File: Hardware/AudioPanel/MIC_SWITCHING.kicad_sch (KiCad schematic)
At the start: 18 parts, among them SW8 ~{RESET}, U119 ADG729, U120 ADG729, U30 MCP23017_ML, U60 MCP23017_ML

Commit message: Added MIC PTT UP DOWN sensing and buffering
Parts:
- removed C141, C142: 100nF, symbol Device:C_Small
- removed C143: 10uF, symbol Device:C_Polarized_Small_US
- removed SW8: ~{RESET}, Button_Switch_SMD:SW_SPST_TL3342, symbol Switch:SW_Push
- removed U30: MCP23017_ML, Package_DFN_QFN:QFN-28-1EP_6x6mm_P0.65mm_EP4.25x4.25mm, symbol Interface_Expansion:MCP23017_ML
- added C129: 100nF, symbol Device:C_Small
- added C70: 10uF, symbol Device:C_Polarized_Small_US
- added R103, R361, R362: 10k, symbol Device:R_Small_US
- added R363, R364, R365, R369, R371, R372, R375, R376, R379, R380, R381, R382, R387, R388, R389, R390, R395, R396, R397, R398, R399, R400, R401, R402: 2k, symbol Device:R_Small_US
- added R366, R367, R368, R370, R373, R374, R377, R378, R383, R384, R385, R386, R391, R392, R393, R394: 1k, symbol Device:R_Small_US
- added U121, U58: LM339, symbol Comparator:LM339
- added U122, U124 (x2): MCP6004, symbol Amplifier_Operational:MCP6004
- added U123: MCP23017_ML, Package_DFN_QFN:QFN-28-1EP_6x6mm_P0.65mm_EP4.25x4.25mm, symbol Interface_Expansion:MCP23017_ML
- added U30, U57: 74HC14, symbol AudioPanelLibrary:74HC14
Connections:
- net +5V: now also C120.1, C129.1, C70.1, R103.1, U121.3 (V+), U122.4 (V+), U123.5 (VDD), U124.4 (V+), U30.14 (VCC), U57.14 (VCC), U58.3 (V+)
- net 480_MIC.DN: now also R374.2, U122.8; no longer U60.17 (GPA0)
- net 480_MIC.PTT: now also U60.19 (GPA2)
- net 480_MIC.UP: now also R373.2, U122.14; no longer U60.25 (GPB0)
- net 700_MIC.DN: now also R384.2, U124.8; no longer U60.19 (GPA2)
- net 700_MIC.PTT: now also U60.21 (GPA4)
- net 700_MIC.UP: now also R383.2, U124.14; no longer U60.27 (GPB2)
- net 710_MIC.DN: now also R368.2, U122.7; no longer U60.18 (GPA1)
- net 710_MIC.PTT: now also U60.20 (GPA3)
- net 710_MIC.UP: now also R366.2, U122.1; no longer U60.26 (GPB1)
- net CODRIVER_MIC.DN: now also U58.10 (-), U58.8 (-); no longer U60.23 (GPA6)
- net CODRIVER_MIC.PTT: now also U57.9
- net CODRIVER_MIC.UP: now also U121.10 (-), U121.8 (-); no longer U60.3 (GPB6)
- net DRIVER_MIC.DN: now also U58.4 (-), U58.6 (-); no longer U60.24 (GPA7)
- net DRIVER_MIC.PTT: now also U57.5
- net DRIVER_MIC.UP: now also U121.4 (-), U121.6 (-); no longer U60.4 (GPB7)
- net EXTRA_MIC.DN: now also R386.2, U124.7; no longer U60.20 (GPA3)
- net EXTRA_MIC.PTT: now also U60.22 (GPA5)
- net EXTRA_MIC.UP: now also R385.2, U124.1; no longer U60.28 (GPB3)
- net GND: now also C129.2, C70.2, R362.2, R365.2, R372.2, R381.2, R382.2, R399.2, R400.2, R401.2, R402.2, U121.12 (V-), U122.10 (+), U122.11 (V-), U122.12 (+), U122.3 (+), U122.5 (+), U123.11 (A0), U123.12 (A1), U123.13 (A2), U123.29 (EP), U123.6 (VSS), U124.10 (+), U124.11 (V-), U124.12 (+), U124.3 (+), U124.5 (+), U30.7 (GND), U57.7 (GND), U58.12 (V-)
- net INTA1: now also U123.16 (INTA)
- net INTB1: now also U123.15 (INTB)
- net SCL: now also U123.8 (SCK)
- net SDA: now also U123.9 (SDA)
- net ~{RESET}: now also U123.14 (~{RESET}); no longer C120.1
- net CODRIVER_UP_MSB: now reaches U60.1 (GPB4)
- net CODRIVER_UP_MSB: now also U30.6
- net CODRIVER_UP_LSB: now reaches U60.2 (GPB5)
- net CODRIVER_UP_LSB: now also U30.8
- new net: R386.1, R390.1, R394.1, U124.6 (-)
- new net: R378.2, R380.1, R382.1
- new net: R385.1, R389.1, R393.1, U124.2 (-)
- new net: R374.1, R376.1, R378.1, U122.9 (-)
- new net: R384.1, R388.1, R392.1, U124.9 (-)
- new net: U121.1, U30.13
- new net: R368.1, R369.1, R370.1, U122.6 (-)
- new net: R370.2, R371.1, R372.1
- new net: U121.14, U57.3
- new net: R392.2, R396.1, R400.1
- new net: R377.2, R379.1, R381.1
- new net: U30.1, U58.2
- new net: R363.1, R366.1, R367.1, U122.2 (-)
- new net: R373.1, R375.1, R377.1, U122.13 (-)
- new net: R364.1, R365.1, R367.2
- new net: U121.13, U57.1
- new net: R383.1, R387.1, R391.1, U124.13 (-)
- new net: R391.2, R395.1, R399.1
- new net: U30.3, U58.1
- new net: R393.2, R397.1, R401.1
- new net: U30.9, U58.14
- new net: R394.2, R398.1, R402.1
- new net: U30.5, U58.13
- new net: U121.2, U30.11
- new net 1V66: R361.2, R362.1, U121.7 (+), U121.9 (+), U58.7 (+), U58.9 (+)
- new net 3V33: R103.2, R361.1, U121.11 (+), U121.5 (+), U58.11 (+), U58.5 (+)
- new net 480_DN_LSB: R380.2, U123.28 (GPB3)
- new net 480_DN_MSB: R376.2, U123.27 (GPB2)
- new net 480_UP_LSB: R379.2, U123.26 (GPB1)
- new net 480_UP_MSB: R375.2, U123.25 (GPB0)
- new net 700_DN_LSB: R396.2, U123.20 (GPA3)
- new net 700_DN_MSB: R388.2, U123.19 (GPA2)
- new net 700_UP_LSB: R395.2, U123.18 (GPA1)
- new net 700_UP_MSB: R387.2, U123.17 (GPA0)
- new net 710_DN_LSB: R371.2, U123.4 (GPB7)
- new net 710_DN_MSB: R369.2, U123.3 (GPB6)
- new net 710_UP_LSB: R364.2, U123.2 (GPB5)
- new net 710_UP_MSB: R363.2, U123.1 (GPB4)
- new net CODRIVER_DN_LSB: U57.4, U60.4 (GPB7)
- new net CODRIVER_DN_MSB: U57.2, U60.3 (GPB6)
- new net DRIVER_DN_LSB: U30.12, U60.28 (GPB3)
- new net DRIVER_DN_MSB: U30.10, U60.27 (GPB2)
- new net DRIVER_UP_LSB: U30.4, U60.26 (GPB1)
- new net DRIVER_UP_MSB: U30.2, U60.25 (GPB0)
- new net EXTRA_DN_LSB: R398.2, U123.24 (GPA7)
- new net EXTRA_DN_MSB: R390.2, U123.23 (GPA6)
- new net EXTRA_UP_LSB: R397.2, U123.22 (GPA5)
- new net EXTRA_UP_MSB: R389.2, U123.21 (GPA4)
- new net ~{CODRIVER_PTT_IN}: U57.8, U60.18 (GPA1)
- new net ~{DRIVER_PTT_IN}: U57.6, U60.17 (GPA0)
- no-connect marks 0 -> 4
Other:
- note added: "Kenwood MIC Up/Down Button Voltage Mapping"
- note added: "Keypress Detection Driver/Codriver Up, Down, PTT"
- note added: "Keypress Generation Driver/Codriver Up, Down, PTT"
- note added: "Microphone Audio Switching"
- note added: "Microphone Input From Driver & Codriver"
- note added: "Microphone Output To All Radios"
- note added: "PTT Pressed = 0V PTT Released = 5V"
- moved on the sheet: C138, C139, C140, C565, C566, C567, C568, C569, C570, U119, U120, U60

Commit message: Replaced microphone page bs with an ADC and DAC
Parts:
- removed C138, C139: 100nF, symbol Device:C_Small
- removed C140: 10uF, symbol Device:C_Polarized_Small_US
- removed R103, R361, R362: 10k, symbol Device:R_Small_US
- removed R363, R364, R365, R369, R371, R372, R375, R376, R379, R380, R381, R382, R387, R388, R389, R390, R395, R396, R397, R398, R399, R400, R401, R402: 2k, symbol Device:R_Small_US
- removed R366, R367, R368, R370, R373, R374, R377, R378, R383, R384, R385, R386, R391, R392, R393, R394: 1k, symbol Device:R_Small_US
- removed U121, U58: LM339, symbol Comparator:LM339
- removed unit 2 of U122
- removed unit 1 of U122
- removed unit 3 of U122
- removed unit 4 of U122
- removed U123, U60: MCP23017_ML, Package_DFN_QFN:QFN-28-1EP_6x6mm_P0.65mm_EP4.25x4.25mm, symbol Interface_Expansion:MCP23017_ML
- removed unit 3 of U124
- removed unit 2 of U124
- removed unit 4 of U124
- removed unit 1 of U124
- removed U30, U57: 74HC14, symbol AudioPanelLibrary:74HC14
- added C130, C133: 10uF, symbol Device:C_Polarized_Small_US
- added C131, C132, C134, C141: 100nF, symbol Device:C_Small
- added U123: ADS7830, Package_SO:TSSOP-16_4.4x5mm_P0.65mm, symbol Analog_DAC:ADS7830
- added U125, U126: MCP47FVB08, symbol AudioPanelLibrary:MCP47FVB08
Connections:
- net +5V: now also C130.1, C131.1, C132.1, C133.1, C134.1, C141.1, U123.12 (A0), U123.13 (A1), U123.16 (VDD), U125.1 (A0), U125.14 (VREF1), U125.2 (VREF0), U125.20 (VDD), U126.14 (VREF1), U126.2 (VREF0), U126.20 (VDD)
- net 480_MIC.DN: now also U125.3 (VOUT0)
- net 480_MIC.PTT: now also U126.3 (VOUT0)
- net 480_MIC.UP: now also U125.13 (VOUT1)
- net 700_MIC.DN: now also U125.5 (VOUT4)
- net 700_MIC.PTT: now also U126.4 (VOUT2)
- net 700_MIC.UP: now also U125.11 (VOUT5)
- net 710_MIC.DN: now also U125.4 (VOUT2)
- net 710_MIC.PTT: now also U126.13 (VOUT1)
- net 710_MIC.UP: now also U125.12 (VOUT3)
- net CODRIVER_MIC.DN: now also U123.6 (CH5)
- net CODRIVER_MIC.PTT: now also U123.8 (CH7)
- net CODRIVER_MIC.UP: now also U123.7 (CH6)
- net DRIVER_MIC.DN: now also U123.1 (CH0)
- net DRIVER_MIC.PTT: now also U123.3 (CH2)
- net DRIVER_MIC.UP: now also U123.2 (CH1)
- net EXTRA_MIC.DN: now also U125.6 (VOUT6)
- net EXTRA_MIC.PTT: now also U126.12 (VOUT3)
- net EXTRA_MIC.UP: now also U125.10 (VOUT7)
- net GND: now also C130.2, C131.2, C132.2, C133.2, C134.2, C141.2, U123.11 (COM), U123.9 (GND), U125.15 (A1), U125.7 (VSS), U126.1 (A0), U126.15 (A1), U126.7 (VSS)
- net SCL: now also U123.14 (SCL), U125.16 (SCL), U126.16 (SCL)
- net SDA: now also U123.15 (SDA), U125.17 (SDA), U126.17 (SDA)
- no-connect marks 4 -> 0
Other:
- note added: "0x4B"
- note added: "0x60"
- note added: "0x61"
- note removed: "0x20"
- note removed: "0x21"
- moved on the sheet: C120, C129, C70

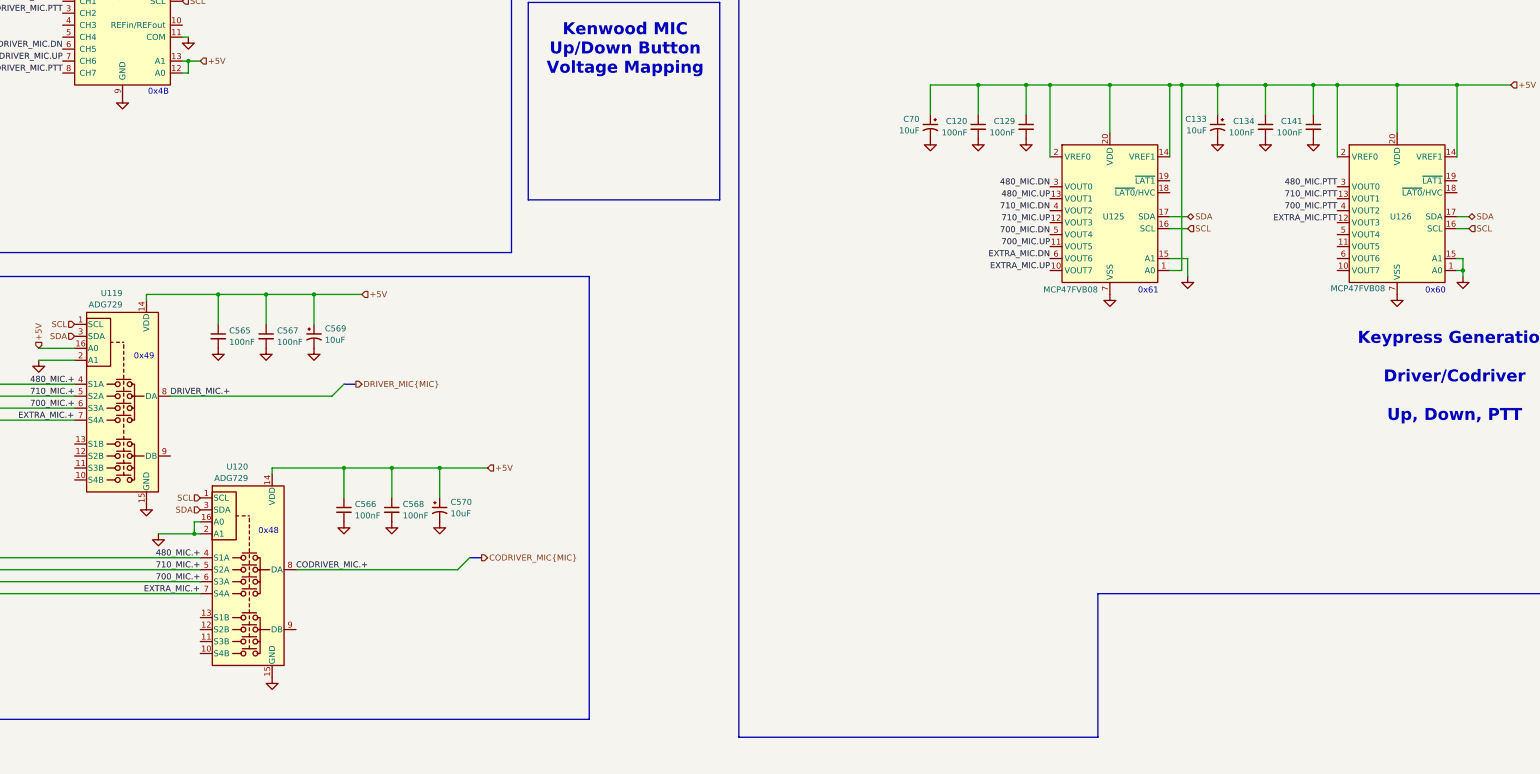
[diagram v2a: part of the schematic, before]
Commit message: Adding ADAV400 sheet
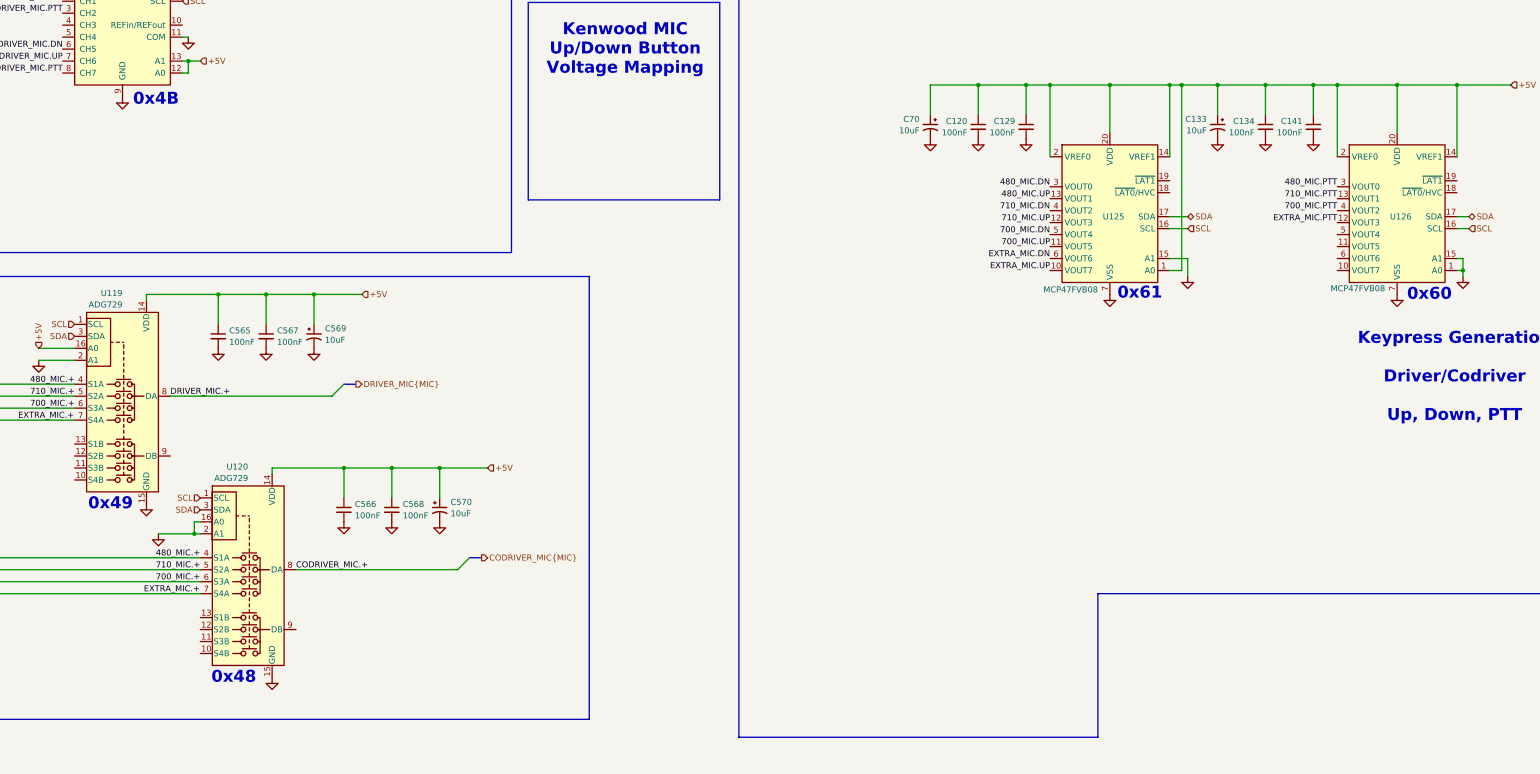
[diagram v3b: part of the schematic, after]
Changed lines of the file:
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@@
 	(text "0x4B"
 		(exclude_from_sim no)
-		(at 111.76 128.524 0)
+		(at 111.252 130.048 0)
 		(effects
 			(font
-				(size 1.27 1.27)
+				(size 2.54 2.54)
+				(thickness 0.508)
+				(bold yes)
 			)
 		)
@@
 	(text "0x60"
 		(exclude_from_sim no)
-		(at 382.778 170.688 0)
+		(at 381.508 171.45 0)
 		(effects
 			(font
-				(size 1.27 1.27)
+				(size 2.54 2.54)
+				(thickness 0.508)
+				(bold yes)
 			)
 		)
@@
 	(text "0x61"
 		(exclude_from_sim no)
-		(at 321.818 170.688 0)
+		(at 320.04 171.196 0)
 		(effects
 			(font
-				(size 1.27 1.27)
+				(size 2.54 2.54)
+				(thickness 0.508)
+				(bold yes)
 			)
 		)
@@
 	(text "0x49"
 		(exclude_from_sim no)
-		(at 108.712 184.658 0)
+		(at 101.6 215.9 0)
 		(effects
 			(font
-				(size 1.27 1.27)
+				(size 2.54 2.54)
+				(thickness 0.508)
+				(bold yes)
 			)
 		)
@@
 	(text "0x48"
 		(exclude_from_sim no)
-		(at 135.128 221.742 0)
+		(at 127.762 252.73 0)
 		(effects
 			(font
-				(size 1.27 1.27)
+				(size 2.54 2.54)
+				(thickness 0.508)
+				(bold yes)
 			)
 		)
